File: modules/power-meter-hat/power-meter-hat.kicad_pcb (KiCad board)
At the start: 2 copper layers, 65 x 56 mm, 42 parts, among them J1 GPIO, J2 Conn_01x02, J3 Conn_01x02, J4 Conn_01x02, U1 CAT24C256, U2 INA219AxD, U3 INA219AxD, U4 INA219AxD

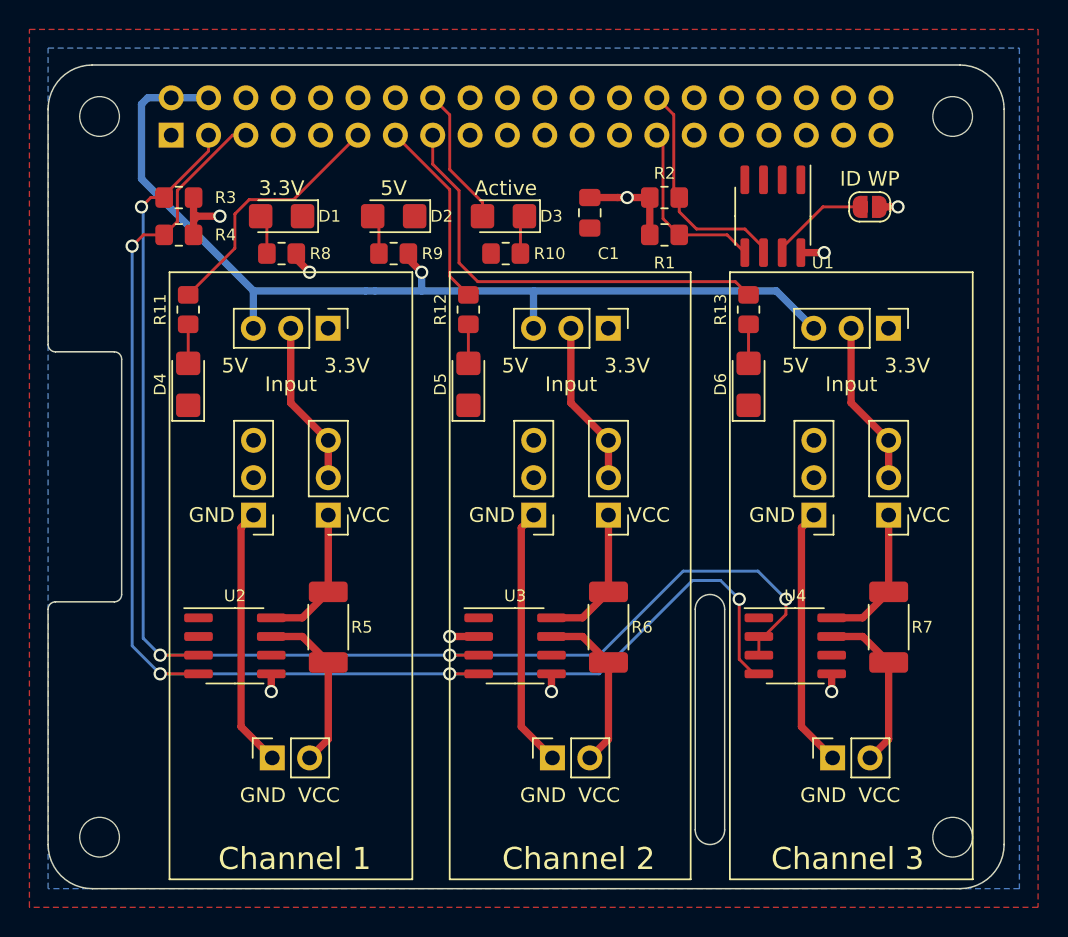
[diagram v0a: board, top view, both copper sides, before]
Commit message: Add external power source
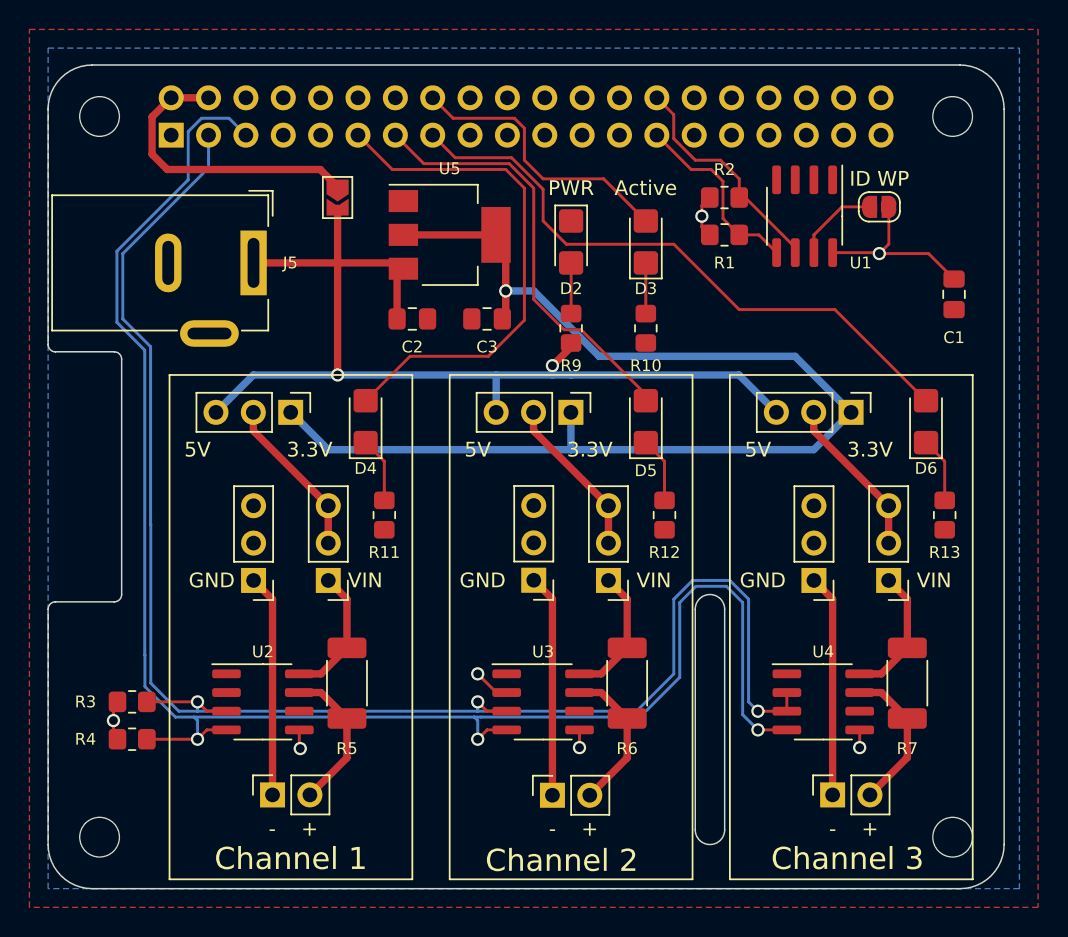
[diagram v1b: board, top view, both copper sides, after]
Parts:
- removed D1: LED, LED_SMD:LED_1206_3216Metric_Castellated
- removed R8: R, Resistor_SMD:R_0805_2012Metric_Pad1.20x1.40mm_HandSolder
- added C2: 22u, Capacitor_SMD:C_0805_2012Metric_Pad1.18x1.45mm_HandSolder, F.Cu at (124.8, 61.3)
- added C3: 22u, Capacitor_SMD:C_0805_2012Metric_Pad1.18x1.45mm_HandSolder, F.Cu at (129.8, 61.3)
- added J5: Barrel_Jack_Switch, Connector_BarrelJack:BarrelJack_Wuerth_6941xx301002, F.Cu at (114.0, 57.5)
- added JP11: Jumper, Jumper:SolderJumper-2_P1.3mm_Open_TrianglePad1.0x1.5mm, F.Cu at (119.7, 53.0)
- added U5: NCP1117-3.3_SOT223, Package_TO_SOT_SMD:SOT-223-3_TabPin2, F.Cu at (127.3, 55.5)
- R10, R11, R12, R13, R9: value R -> 220R
- R3, R4: value R -> 10k
- R5, R6, R7: value R -> ?
- moved R4 34.4 mm to (105.7, 89.8), turned to 0 degrees
- moved R3 34.4 mm to (105.7, 87.3), turned to 0 degrees
- moved C1 25.4 mm to (161.6, 59.6)
- moved R12 19.3 mm to (141.9, 74.6)
- moved R13 19.3 mm to (161.0, 74.6)
- moved R11 19.3 mm to (122.9, 74.6)
- moved R9 13.1 mm to (135.6, 61.9), turned to -90 degrees
- moved D4 12.3 mm to (121.6, 68.2)
- moved D5 12.3 mm to (140.6, 68.2)
- moved D6 12.3 mm to (159.7, 68.2)
- moved D2 12.2 mm to (135.6, 56.0), turned to -90 degrees
- moved R10 10.8 mm to (140.6, 61.9), turned to 90 degrees
- moved D3 9.84 mm to (140.6, 56.0), turned to 90 degrees
- moved JP7 6.25 mm to (135.5, 67.6)
- moved JP10 6.25 mm to (154.6, 67.6)
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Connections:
- D4 pad 1: GND -> Net-(R11-Pad2)
- D4 pad 2: Net-(D4-Pad2) -> /GPIO[17]
- D5 pad 1: GND -> Net-(R12-Pad2)
- D5 pad 2: Net-(D5-Pad2) -> /GPIO[27]
- D6 pad 1: GND -> Net-(R13-Pad2)
- D6 pad 2: Net-(D6-Pad2) -> /GPIO[22]
- JP10 pad 1: +3V3 -> +3.3VP
- JP10 pad 3: +5V -> +5VP
- JP4 pad 1: +3V3 -> +3.3VP
- JP4 pad 3: +5V -> +5VP
- JP7 pad 1: +3V3 -> +3.3VP
- JP7 pad 3: +5V -> +5VP
- R11 pad 1: Net-(D4-Pad2) -> GND
- R11 pad 2: /GPIO[17] -> Net-(R11-Pad2)
- R12 pad 1: Net-(D5-Pad2) -> GND
- R12 pad 2: /GPIO[27] -> Net-(R12-Pad2)
- R13 pad 1: Net-(D6-Pad2) -> GND
- R13 pad 2: /GPIO[22] -> Net-(R13-Pad2)
- R9 pad 2: +5V -> +5VP
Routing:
- net +3.3VP: track 0.00 -> 82.0 mm, vias 0 -> 1
- net +5VP: track 0.00 -> 70.7 mm, vias 0 -> 2
- net +5V: track 67.7 -> 20.4 mm, vias 1 -> 0
- net /SCL: track 94.9 -> 116.1 mm, vias 4 -> 3
- net /GPIO[17]: track 17.4 -> 34.8 mm
- net /GPIO[27]: track 12.9 -> 29.2 mm
- net /SDA: track 93.3 -> 109.4 mm, vias 4 -> 3
- net /GPIO[22]: track 30.0 -> 42.3 mm
- net /GPIO[23]: track 9.45 -> 19.2 mm
- net Net-(R13-Pad2): track 0.00 -> 4.45 mm
- net Net-(R12-Pad2): track 0.00 -> 4.45 mm
- net Net-(R11-Pad2): track 0.00 -> 4.45 mm
- net +3V3: track 21.2 -> 24.4 mm, vias 9 -> 7
- net Net-(D1-Pad2): track 2.72 -> 0.00 mm
- net Net-(D6-Pad2): track 2.65 -> 0.00 mm
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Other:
- board text added: "+"
- board text added: "-"
- board text removed: "GND"
- board text removed: "VCC"

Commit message: Replace pin sockets with screw terminals
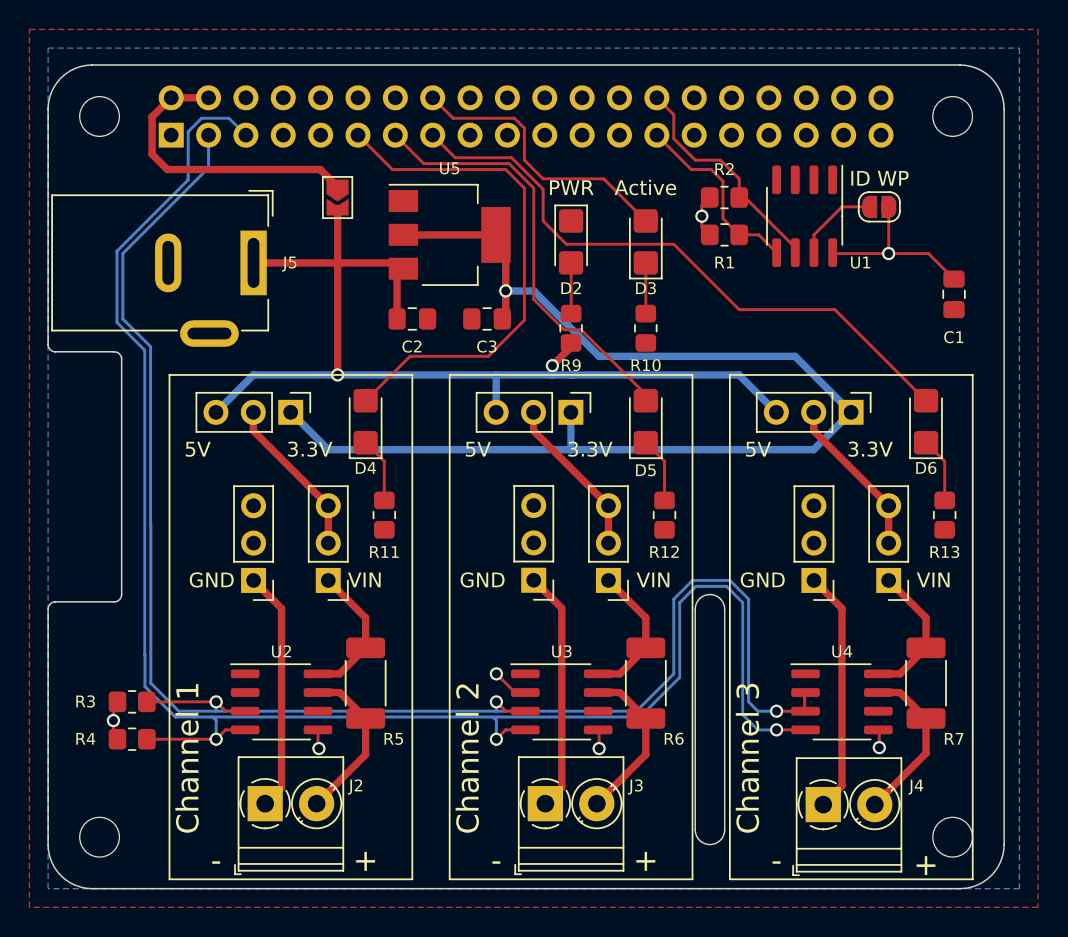
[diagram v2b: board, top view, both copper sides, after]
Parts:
- J2, J3, J4: footprint Connector_PinSocket_2.54mm:PinSocket_1x02_P2.54mm_Vertical -> TerminalBlock_Phoenix:TerminalBlock_Phoenix_PT-1,5-2-3.5-H_1x02_P3.50mm_Horizontal
- moved R5 1.27 mm to (121.6, 86.0)
- moved R7 1.27 mm to (159.7, 86.0)
- moved U3 1.27 mm to (134.9, 87.3)
- moved U2 1.27 mm to (115.9, 87.3)
- moved R6 1.27 mm to (140.6, 86.0)
- moved U4 1.27 mm to (154.0, 87.3)
- moved J4 0.92 mm to (152.7, 94.3), turned to 0 degrees
- moved J2 0.78 mm to (114.8, 94.2), turned to 0 degrees
- moved J3 0.75 mm to (133.8, 94.2), turned to 0 degrees
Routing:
- net /SCL: track 116.1 -> 118.6 mm
- net /SDA: track 109.4 -> 111.9 mm
- net /PowerChannel 3/OUT_GND: track 15.1 -> 16.6 mm
- net /PowerChannel 1/OUT_GND: track 15.1 -> 16.4 mm
- net /PowerChannel 2/OUT_GND: track 15.1 -> 16.4 mm
- net /PowerChannel 3/OUT_VCC: track 10.2 -> 11.3 mm
- net /PowerChannel 1/OUT_VCC: track 10.2 -> 11.1 mm
- net /PowerChannel 2/OUT_VCC: track 10.2 -> 11.1 mm
- net /PowerChannel 3/IN_VCC: track 9.08 -> 9.61 mm
- net /PowerChannel 1/IN_VCC: track 9.08 -> 9.61 mm
- net /PowerChannel 2/IN_VCC: track 9.08 -> 9.61 mm

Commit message: Reannotate schematic
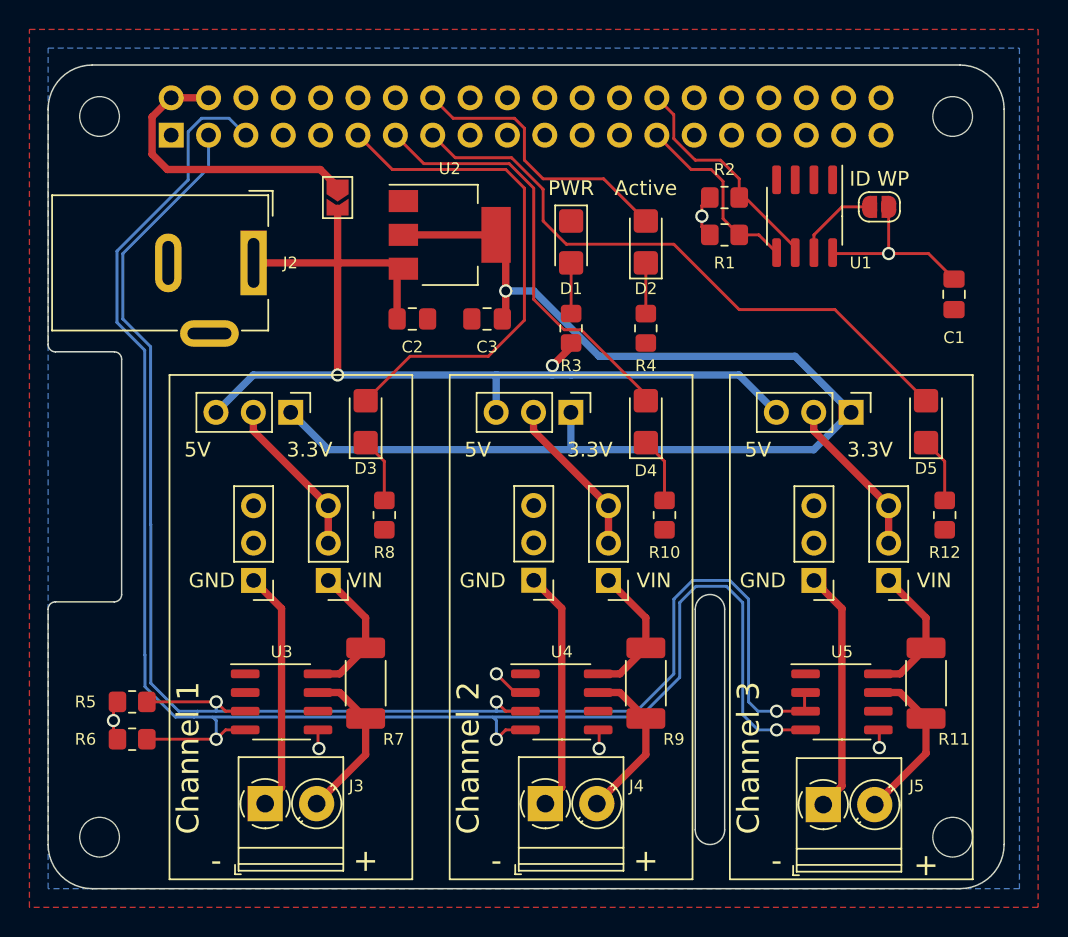
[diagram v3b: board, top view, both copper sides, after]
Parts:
- renumbered D2 to D1, D3 to D2, D4 to D3, D5 to D4, D6 to D5, J5 to J2, J2 to J3, J3 to J4, J4 to J5, JP9 to JP10, JP10 to JP11, JP11 to JP2, JP2 to JP3, JP3 to JP4, JP4 to JP5, JP5 to JP6, JP6 to JP7, JP7 to JP8, JP8 to JP9, R12 to R10, R7 to R11, R13 to R12, R9 to R3, R10 to R4, R3 to R5, R4 to R6, R5 to R7, R11 to R8, R6 to R9, U5 to U2, U2 to U3, U3 to U4, U4 to U5

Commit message: Replace barrel jack to CLIFF FC68148
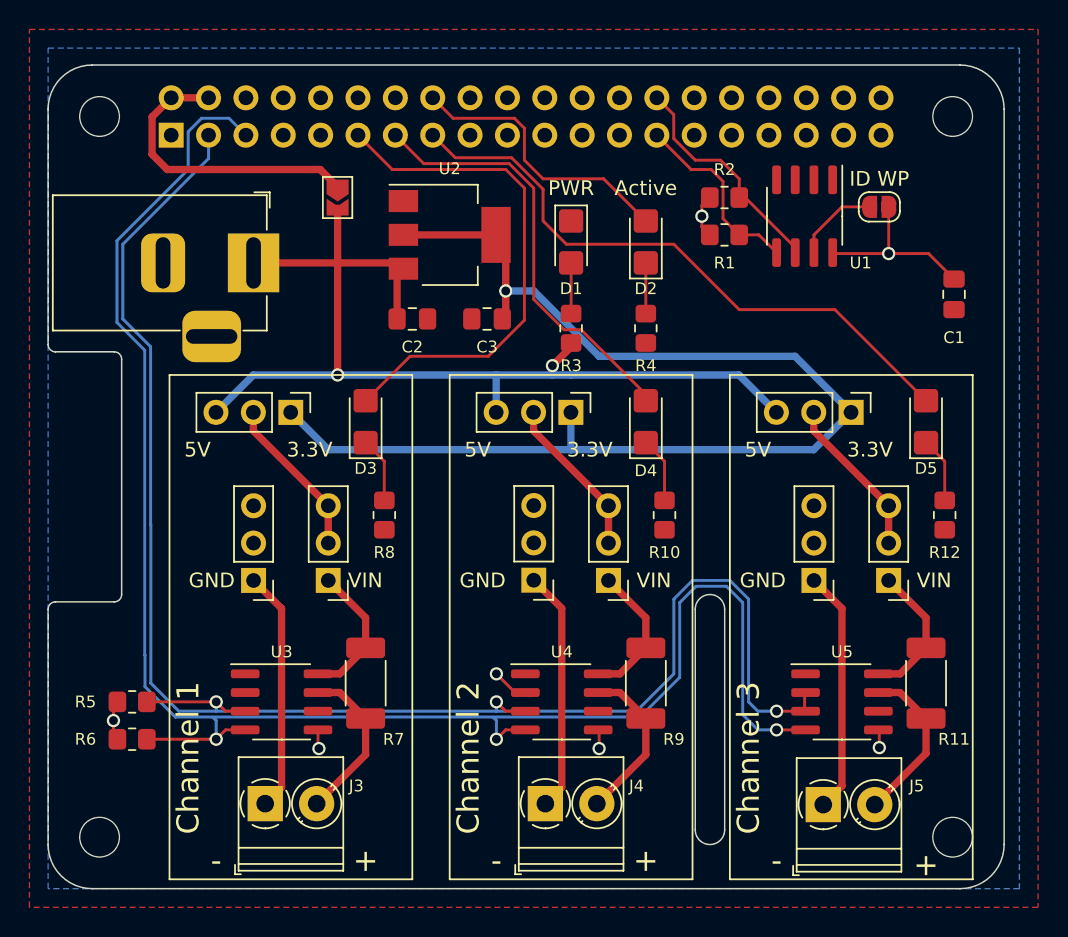
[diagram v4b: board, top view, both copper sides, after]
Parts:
- J2: footprint Connector_BarrelJack:BarrelJack_Wuerth_6941xx301002 -> shared_components:BarrelJack_CLIFF_FC68148_Horizontal
- turned J2 to 0 degrees
